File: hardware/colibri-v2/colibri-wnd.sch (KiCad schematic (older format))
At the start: 0 parts

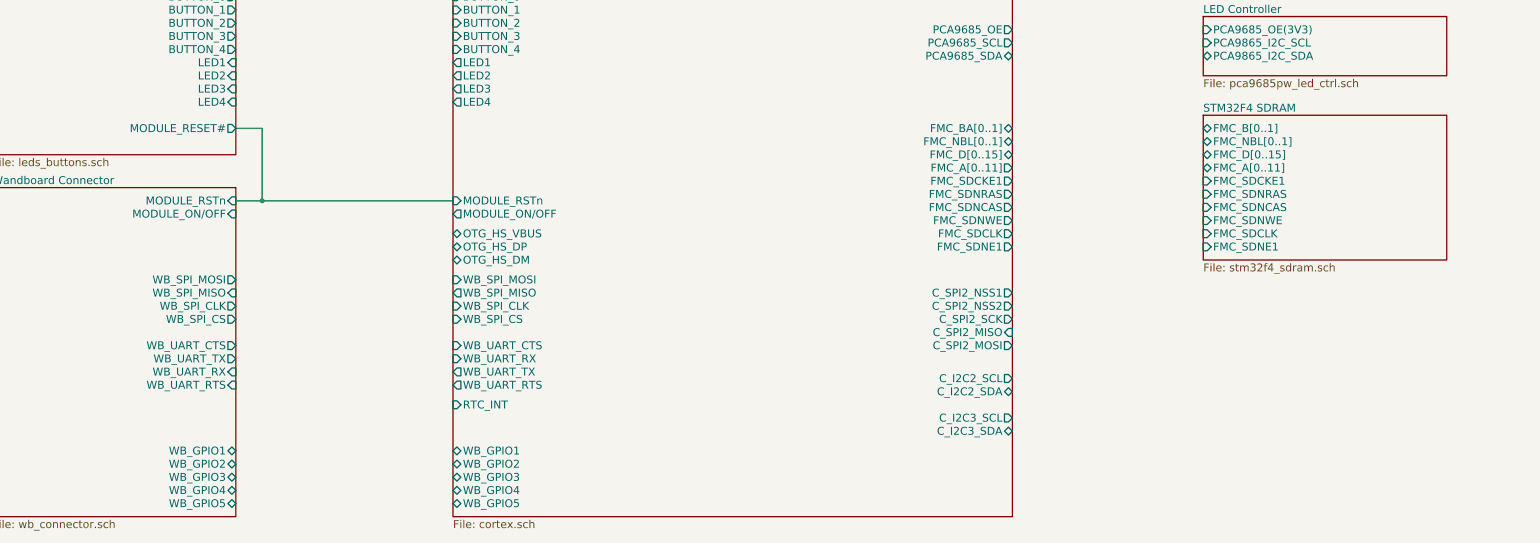
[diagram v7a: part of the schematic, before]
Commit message: Added ext_sensors.sch sheet
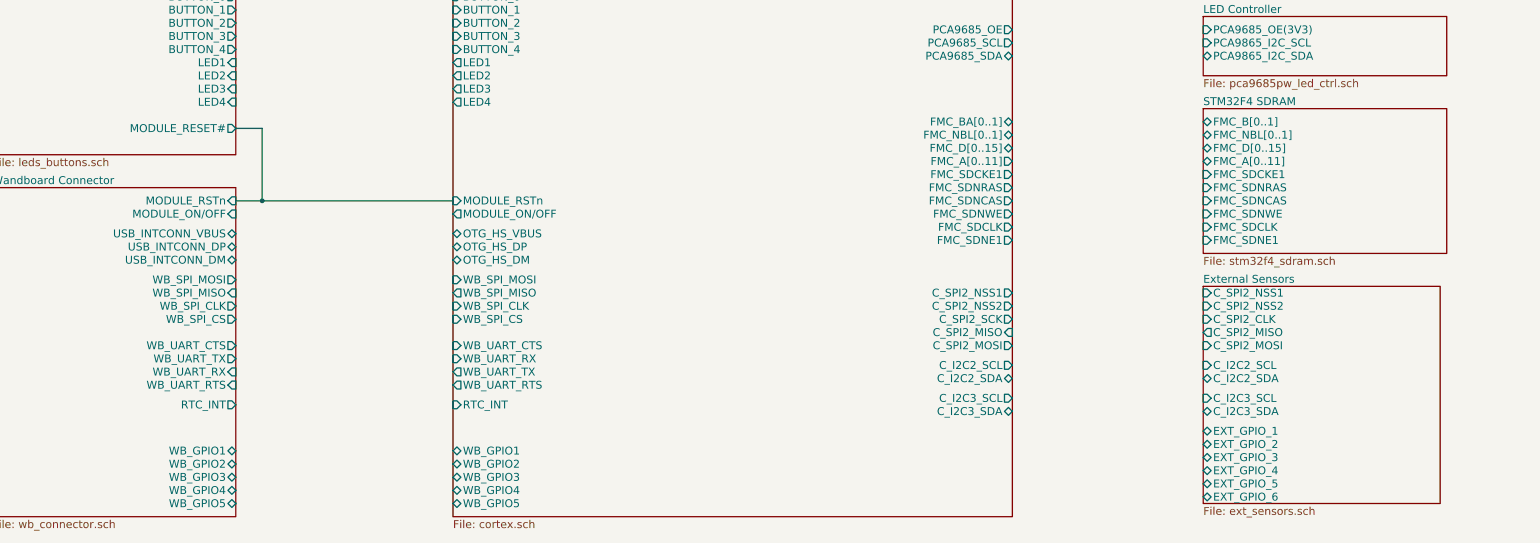
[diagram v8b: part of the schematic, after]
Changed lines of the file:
@@
 $EndSheet
 $Sheet
-S 12700 6900 1850 1100
+S 12700 6850 1850 1100
 U 55895050
 F0 "STM32F4 SDRAM" 60
 F1 "stm32f4_sdram.sch" 60
-F2 "FMC_B[0..1]" B L 12700 7000 60
-F3 "FMC_SDNE1" I L 12700 7900 60
-F4 "FMC_SDNWE" I L 12700 7700 60
-F5 "FMC_SDNRAS" I L 12700 7500 60
-F6 "FMC_SDNCAS" I L 12700 7600 60
-F7 "FMC_SDCLK" I L 12700 7800 60
-F8 "FMC_SDCKE1" I L 12700 7400 60
-F9 "FMC_NBL[0..1]" B L 12700 7100 60
-F10 "FMC_D[0..15]" B L 12700 7200 60
-F11 "FMC_A[0..11]" B L 12700 7300 60
+F2 "FMC_B[0..1]" B L 12700 6950 60
+F3 "FMC_SDNE1" I L 12700 7850 60
+F4 "FMC_SDNWE" I L 12700 7650 60
+F5 "FMC_SDNRAS" I L 12700 7450 60
+F6 "FMC_SDNCAS" I L 12700 7550 60
+F7 "FMC_SDCLK" I L 12700 7750 60
+F8 "FMC_SDCKE1" I L 12700 7350 60
+F9 "FMC_NBL[0..1]" B L 12700 7050 60
+F10 "FMC_D[0..15]" B L 12700 7150 60
+F11 "FMC_A[0..11]" B L 12700 7250 60
 $EndSheet
 $Sheet
@@
 F15 "WB_GPIO4" B R 5350 9750 60
 F16 "WB_GPIO5" B R 5350 9850 60
+F17 "RTC_INT" O R 5350 9100 60
+F18 "USB_INTCONN_VBUS" B R 5350 7800 60
+F19 "USB_INTCONN_DM" B R 5350 8000 60
+F20 "USB_INTCONN_DP" B R 5350 7900 60
 $EndSheet
 $Sheet
@@
 F76 "PWR_BTN_READ" I L 7000 3900 60
 F77 "PWR_ON" O L 7000 4300 60
-F78 "C_I2C2_SCL" O R 11250 8900 60
-F79 "C_I2C2_SDA" B R 11250 9000 60
-F80 "C_I2C3_SCL" O R 11250 9200 60
-F81 "C_I2C3_SDA" B R 11250 9300 60
-F82 "FMC_SDCKE1" O R 11250 7400 60
-F83 "FMC_SDNE1" O R 11250 7900 60
-F84 "FMC_SDNWE" O R 11250 7700 60
-F85 "FMC_NBL[0..1]" B R 11250 7100 60
-F86 "FMC_SDNRAS" O R 11250 7500 60
-F87 "FMC_BA[0..1]" B R 11250 7000 60
-F88 "FMC_SDCLK" O R 11250 7800 60
-F89 "FMC_SDNCAS" O R 11250 7600 60
-F90 "FMC_A[0..11]" O R 11250 7300 60
-F91 "FMC_D[0..15]" B R 11250 7200 60
+F78 "C_I2C2_SCL" O R 11250 8800 60
+F79 "C_I2C2_SDA" B R 11250 8900 60
+F80 "C_I2C3_SCL" O R 11250 9050 60
+F81 "C_I2C3_SDA" B R 11250 9150 60
+F82 "FMC_SDCKE1" O R 11250 7350 60
+F83 "FMC_SDNE1" O R 11250 7850 60
+F84 "FMC_SDNWE" O R 11250 7650 60
+F85 "FMC_NBL[0..1]" B R 11250 7050 60
+F86 "FMC_SDNRAS" O R 11250 7450 60
+F87 "FMC_BA[0..1]" B R 11250 6950 60
+F88 "FMC_SDCLK" O R 11250 7750 60
+F89 "FMC_SDNCAS" O R 11250 7550 60
+F90 "FMC_A[0..11]" O R 11250 7250 60
+F91 "FMC_D[0..15]" B R 11250 7150 60
 F92 "MEMS_SPI5_SCK" O L 7000 2050 60
 F93 "MEMS_SPI5_MISO" I L 7000 2250 60
@@
 F100 "C_SPI2_NSS2" O R 11250 8350 60
 $EndSheet
+$Sheet
+S 12700 8200 1800 1650
+U 56D05FD4
+F0 "External Sensors" 60
+F1 "ext_sensors.sch" 60
+F2 "C_SPI2_MOSI" I L 12700 8650 60
+F3 "C_SPI2_MISO" O L 12700 8550 60
+F4 "C_SPI2_CLK" I L 12700 8450 60
+F5 "C_SPI2_NSS2" I L 12700 8350 60
+F6 "C_SPI2_NSS1" I L 12700 8250 60
+F7 "C_I2C2_SDA" B L 12700 8900 60
+F8 "C_I2C2_SCL" I L 12700 8800 60
+F9 "C_I2C3_SDA" B L 12700 9150 60
+F10 "C_I2C3_SCL" I L 12700 9050 60
+F11 "EXT_GPIO_1" B L 12700 9300 60
+F12 "EXT_GPIO_2" B L 12700 9400 60
+F13 "EXT_GPIO_3" B L 12700 9500 60
+F14 "EXT_GPIO_4" B L 12700 9600 60
+F15 "EXT_GPIO_5" B L 12700 9700 60
+F16 "EXT_GPIO_6" B L 12700 9800 60
+$EndSheet
 $EndSCHEMATC
